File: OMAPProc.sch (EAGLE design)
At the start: 41 parts, among them IC1 MIC5335-SPYMT, IC2 MIC5335-MGYMT, IC3 TXS0108ERGY, SW1 PWRON, SW2 RESET, SW3 USER

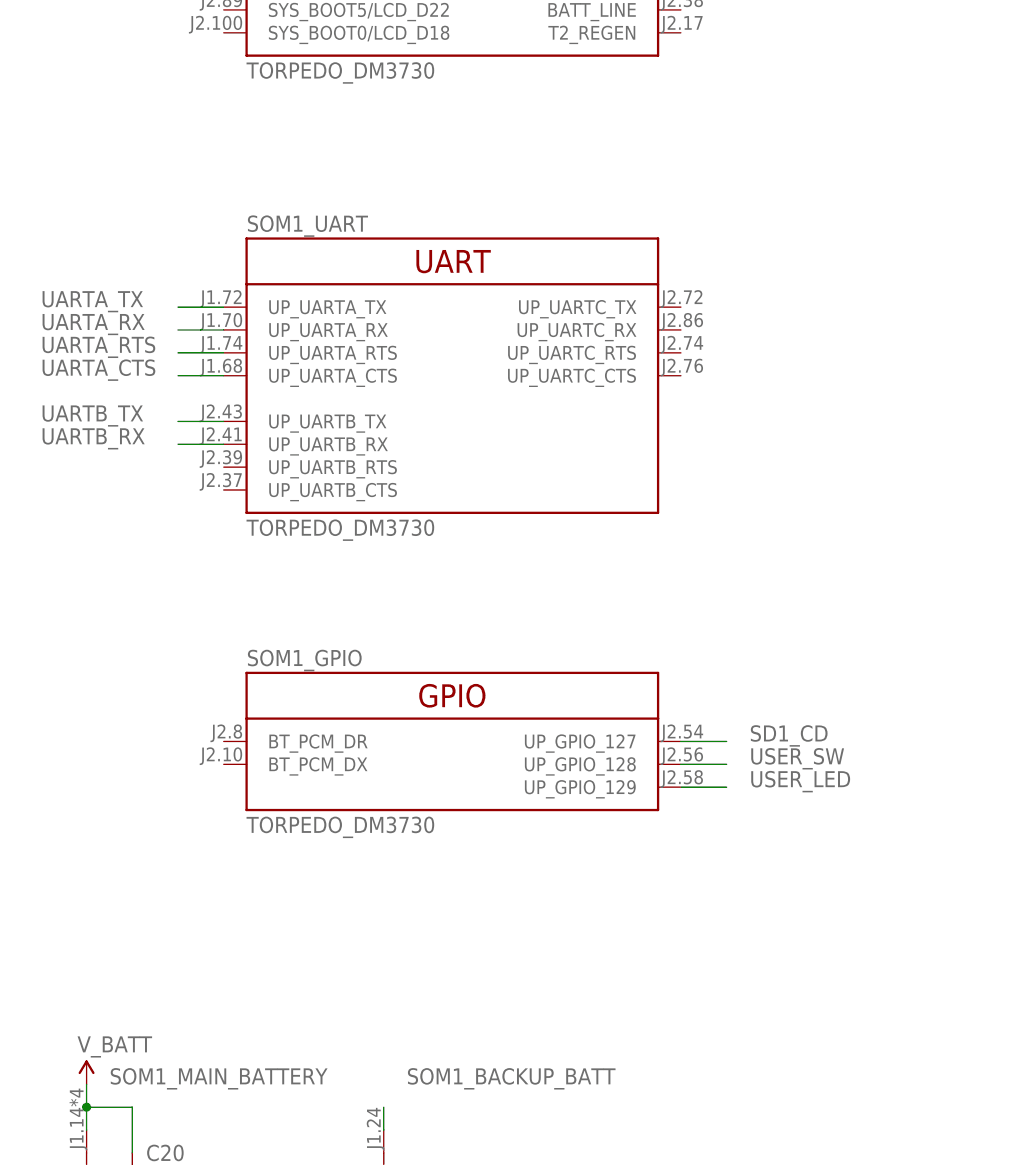
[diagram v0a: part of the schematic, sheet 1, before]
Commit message: Add USB connector
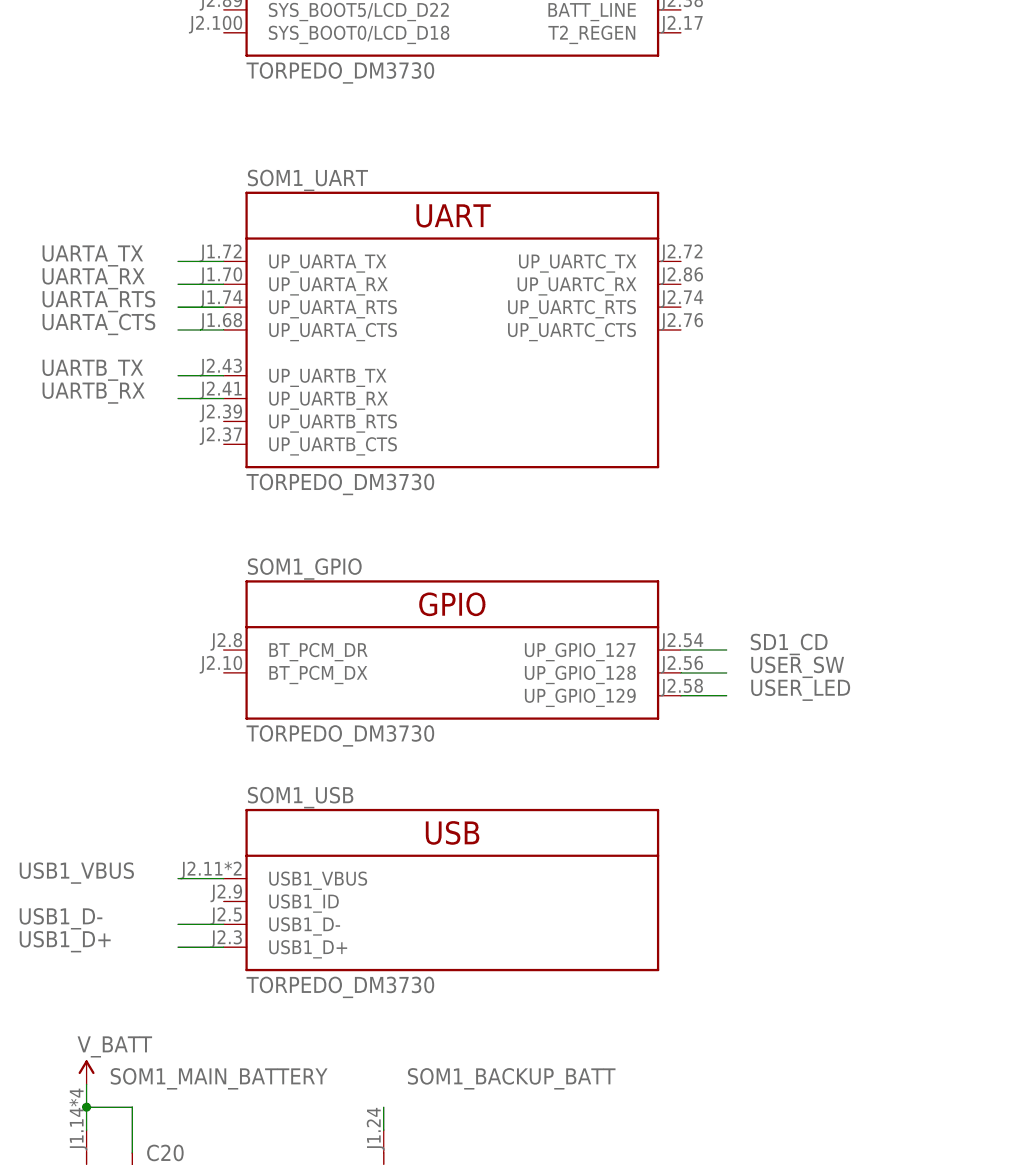
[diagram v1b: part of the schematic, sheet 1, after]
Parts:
- added JP3: USB, biomimetic:MOLEX_503480-0600
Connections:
- new net USB1_D+: JP3.4, SOM1_USB.USB1_D+
- new net USB1_D-: JP3.3, SOM1_USB.USB1_D-
- new net USB1_VBUS: JP3.1, SOM1_USB.USB1_VBUS
- net GND: now also JP3.6
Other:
- moved on the sheet: SOM1_GPIO, SOM1_UART
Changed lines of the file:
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@@
 <attribute name="AUTHOR" value="Ryan Julian (ryanjulian@berkeley.edu)"/>
 <attribute name="DESIGN_NAME" value="OMAPProc"/>
-<attribute name="REVISION" value="A"/>
+<attribute name="REVISION" value="B"/>
 <attribute name="YEAR" value="2012"/>
 </attributes>
@@
 <part name="R9" library="biomimetic" deviceset="RESISTOR" device="0402-RES" value="330"/>
 <part name="GND29" library="biomimetic" deviceset="GND" device=""/>
+<part name="JP3" library="biomimetic" deviceset="MOLEX_503480-0600" device="" value="USB"/>
+<part name="GND30" library="biomimetic" deviceset="GND" device=""/>
 </parts>
 <sheets>
@@
 <instance part="SOM1" gate="_I2C" x="190.5" y="160.02"/>
 <instance part="SOM1" gate="_SDMMC" x="190.5" y="76.2"/>
-<instance part="SOM1" gate="_UART" x="66.04" y="106.68"/>
+<instance part="SOM1" gate="_UART" x="66.04" y="111.76"/>
 <instance part="SOM1" gate="_DGND" x="25.4" y="17.78" smashed="yes">
 <attribute name="NAME" x="27.94" y="5.08" size="1.778" layer="95"/>
@@
 <instance part="R2" gate="G$1" x="137.16" y="152.4"/>
 <instance part="U$3" gate="G$1" x="129.54" y="162.56"/>
-<instance part="SOM1" gate="_GPIO" x="66.04" y="66.04"/>
+<instance part="SOM1" gate="_GPIO" x="66.04" y="76.2"/>
 <instance part="C20" gate="G$1" x="30.48" y="17.78"/>
 <instance part="U$14" gate="G$1" x="25.4" y="27.94"/>
@@
 <attribute name="NAME" x="60.96" y="12.7" size="1.778" layer="95"/>
 </instance>
+<instance part="SOM1" gate="_USB" x="66.04" y="48.26"/>
 </instances>
 <busses>
@@
 <segment>
 <pinref part="SOM1" gate="_GPIO" pin="UP_GPIO_127"/>
-<wire x1="91.44" y1="66.04" x2="96.52" y2="66.04" width="0.1524" layer="91"/>
-<label x="99.06" y="66.04" size="1.778" layer="95"/>
+<wire x1="91.44" y1="76.2" x2="96.52" y2="76.2" width="0.1524" layer="91"/>
+<label x="99.06" y="76.2" size="1.778" layer="95"/>
 </segment>
 </net>
@@
 <segment>
 <pinref part="SOM1" gate="_UART" pin="UP_UARTA_TX"/>
+<wire x1="40.64" y1="119.38" x2="35.56" y2="119.38" width="0.1524" layer="91"/>
+<label x="20.32" y="119.38" size="1.778" layer="95"/>
+</segment>
+</net>
+<net name="UARTA_RX" class="0">
+<segment>
+<pinref part="SOM1" gate="_UART" pin="UP_UARTA_RX"/>
+<wire x1="40.64" y1="116.84" x2="35.56" y2="116.84" width="0.1524" layer="91"/>
+<label x="20.32" y="116.84" size="1.778" layer="95"/>
+</segment>
+</net>
+<net name="UARTA_RTS" class="0">
+<segment>
+<pinref part="SOM1" gate="_UART" pin="UP_UARTA_RTS"/>
 <wire x1="40.64" y1="114.3" x2="35.56" y2="114.3" width="0.1524" layer="91"/>
 <label x="20.32" y="114.3" size="1.778" layer="95"/>
 </segment>
 </net>
-<net name="UARTA_RX" class="0">
-<segment>
-<pinref part="SOM1" gate="_UART" pin="UP_UARTA_RX"/>
+<net name="UARTA_CTS" class="0">
+<segment>
+<pinref part="SOM1" gate="_UART" pin="UP_UARTA_CTS"/>
 <wire x1="40.64" y1="111.76" x2="35.56" y2="111.76" width="0.1524" layer="91"/>
 <label x="20.32" y="111.76" size="1.778" layer="95"/>
 </segment>
 </net>
-<net name="UARTA_RTS" class="0">
-<segment>
-<pinref part="SOM1" gate="_UART" pin="UP_UARTA_RTS"/>
-<wire x1="40.64" y1="109.22" x2="35.56" y2="109.22" width="0.1524" layer="91"/>
-<label x="20.32" y="109.22" size="1.778" layer="95"/>
-</segment>
-</net>
-<net name="UARTA_CTS" class="0">
-<segment>
-<pinref part="SOM1" gate="_UART" pin="UP_UARTA_CTS"/>
+<net name="UARTB_TX" class="0">
+<segment>
+<pinref part="SOM1" gate="_UART" pin="UP_UARTB_TX"/>
 <wire x1="40.64" y1="106.68" x2="35.56" y2="106.68" width="0.1524" layer="91"/>
 <label x="20.32" y="106.68" size="1.778" layer="95"/>
 </segment>
 </net>
-<net name="UARTB_TX" class="0">
-<segment>
-<pinref part="SOM1" gate="_UART" pin="UP_UARTB_TX"/>
-<wire x1="40.64" y1="101.6" x2="35.56" y2="101.6" width="0.1524" layer="91"/>
-<label x="20.32" y="101.6" size="1.778" layer="95"/>
-</segment>
-</net>
 <net name="UARTB_RX" class="0">
 <segment>
 <pinref part="SOM1" gate="_UART" pin="UP_UARTB_RX"/>
-<wire x1="40.64" y1="99.06" x2="35.56" y2="99.06" width="0.1524" layer="91"/>
-<label x="20.32" y="99.06" size="1.778" layer="95"/>
+<wire x1="40.64" y1="104.14" x2="35.56" y2="104.14" width="0.1524" layer="91"/>
+<label x="20.32" y="104.14" size="1.778" layer="95"/>
 </segment>
 </net>
@@
 <segment>
 <pinref part="SOM1" gate="_GPIO" pin="UP_GPIO_128"/>
-<wire x1="91.44" y1="63.5" x2="96.52" y2="63.5" width="0.1524" layer="91"/>
-<label x="99.06" y="63.5" size="1.778" layer="95"/>
+<wire x1="91.44" y1="73.66" x2="96.52" y2="73.66" width="0.1524" layer="91"/>
+<label x="99.06" y="73.66" size="1.778" layer="95"/>
 </segment>
 </net>
@@
 <segment>
 <pinref part="SOM1" gate="_GPIO" pin="UP_GPIO_129"/>
-<wire x1="91.44" y1="60.96" x2="96.52" y2="60.96" width="0.1524" layer="91"/>
-<label x="99.06" y="60.96" size="1.778" layer="95"/>
+<wire x1="91.44" y1="71.12" x2="96.52" y2="71.12" width="0.1524" layer="91"/>
+<label x="99.06" y="71.12" size="1.778" layer="95"/>
+</segment>
+</net>
+<net name="USB1_VBUS" class="0">
+<segment>
+<pinref part="SOM1" gate="_USB" pin="USB1_VBUS"/>
+<wire x1="40.64" y1="50.8" x2="35.56" y2="50.8" width="0.1524" layer="91"/>
+<label x="17.78" y="50.8" size="1.778" layer="95"/>
+</segment>
+</net>
+<net name="USB1_D-" class="0">
+<segment>
+<pinref part="SOM1" gate="_USB" pin="USB1_D-"/>
+<wire x1="40.64" y1="45.72" x2="35.56" y2="45.72" width="0.1524" layer="91"/>
+<label x="17.78" y="45.72" size="1.778" layer="95"/>
+</segment>
+</net>
+<net name="USB1_D+" class="0">
+<segment>
+<pinref part="SOM1" gate="_USB" pin="USB1_D+"/>
+<wire x1="40.64" y1="43.18" x2="35.56" y2="43.18" width="0.1524" layer="91"/>
+<label x="17.78" y="43.18" size="1.778" layer="95"/>
 </segment>
 </net>
@@
 </instance>
 <instance part="GND23" gate="1" x="27.94" y="132.08"/>
+<instance part="JP3" gate="G$1" x="121.92" y="88.9" rot="R180"/>
+<instance part="GND30" gate="1" x="111.76" y="76.2"/>
 </instances>
 <busses>
@@
 <wire x1="27.94" y1="137.16" x2="27.94" y2="134.62" width="0.1524" layer="91"/>
 <pinref part="GND23" gate="1" pin="GND"/>
+</segment>
+<segment>
+<pinref part="JP3" gate="G$1" pin="6"/>
+<wire x1="114.3" y1="81.28" x2="111.76" y2="81.28" width="0.1524" layer="91"/>
+<pinref part="GND30" gate="1" pin="GND"/>
+<wire x1="111.76" y1="78.74" x2="111.76" y2="81.28" width="0.1524" layer="91"/>
 </segment>
 </net>
@@
 </segment>
 </net>
+<net name="USB1_VBUS" class="0">
+<segment>
+<pinref part="JP3" gate="G$1" pin="1"/>
+<wire x1="114.3" y1="93.98" x2="111.76" y2="93.98" width="0.1524" layer="91"/>
+<label x="96.52" y="93.98" size="1.778" layer="95"/>
+</segment>
+</net>
+<net name="USB1_D-" class="0">
+<segment>
+<pinref part="JP3" gate="G$1" pin="3"/>
+<wire x1="114.3" y1="88.9" x2="111.76" y2="88.9" width="0.1524" layer="91"/>
+<label x="96.52" y="88.9" size="1.778" layer="95"/>
+</segment>
+</net>
+<net name="USB1_D+" class="0">
+<segment>
+<pinref part="JP3" gate="G$1" pin="4"/>
+<wire x1="114.3" y1="86.36" x2="111.76" y2="86.36" width="0.1524" layer="91"/>
+<label x="96.52" y="86.36" size="1.778" layer="95"/>
+</segment>
+</net>
